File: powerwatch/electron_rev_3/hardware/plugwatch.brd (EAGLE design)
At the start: 57.1 x 93 mm, 123 parts, among them J1 DM3AT-SF-PEJM5, J2 TC2030-JLINK-NL, U1 BGA725L6-ALT, U10 SIP32510, U11 SIP32510, U12 SIP32510, U13 SIP32510, U14 MPU-9250, U15 OPA322AIDBVT, U2 SAFFB1G56KB0F0A, U3 ISL29035, U4 MAX-M8, U5 MAX740XESA, U6 SIP32510, U7 NRF51822QF, U8 OPA322AIDBVT, U9 SIP32510, X1 32.768k, X2 16MHz

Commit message: small changes
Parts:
- moved U$3 15.0 mm to (32.5, 1.02)
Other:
- board text added: "PowerWatch Noah Klugman Branden Ghena Neal Jackson Josh Adkins Rev 3, 03/18"
- board text removed: "Noah Klugman Branden Ghena Neal Jackson Rev 3 03/18"
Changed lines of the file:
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@@
 <?xml version="1.0" encoding="utf-8"?>
 <!DOCTYPE eagle SYSTEM "eagle.dtd">
-<eagle version="8.5.1">
+<eagle version="8.7.1">
 <drawing>
 <settings>
@@
 <wire x1="43.561" y1="23.368" x2="45.466" y2="23.368" width="0.127" layer="21"/>
 <text x="44.704" y="53.34" size="0.8128" layer="25" font="vector" ratio="12" rot="R270" align="bottom-center">!LIGHT_INT</text>
-<text x="28.448" y="4.064" size="1.016" layer="25" font="vector" ratio="12">Noah Klugman
+<text x="39.624" y="1.016" size="1.016" layer="25" font="vector" ratio="12">PowerWatch
+Noah Klugman
 Branden Ghena
 Neal Jackson
-Rev 3
-03/18</text>
+Josh Adkins
+Rev 3, 03/18</text>
 <text x="44.704" y="90.424" size="0.8128" layer="25" font="vector" ratio="12" align="bottom-center">WIFI_PWR_EN</text>
 <text x="46.736" y="41.656" size="0.8128" layer="25" font="vector" ratio="12" rot="R180" align="bottom-center">AUDIO_OUT</text>
@@
 <text x="8.89" y="52.578" size="0.8128" layer="25" font="vector" ratio="12" rot="R270" align="bottom-center">BLE_TXD</text>
 <text x="9.144" y="20.32" size="1.27" layer="25" font="vector" ratio="12" align="bottom-center">SD CARD</text>
-<text x="47.498" y="73.914" size="1.778" layer="25" font="vector" ratio="12">APN</text>
+<text x="47.752" y="73.914" size="1.778" layer="25" font="vector" ratio="12">APN</text>
 <text x="47.752" y="72.644" size="0.8128" layer="25" font="vector" ratio="12">(on, on)</text>
 </plain>
@@
 <attribute name="VALUE" x="23.622" y="34.036" size="1.016" layer="27" font="vector" ratio="12" align="bottom-center"/>
 </element>
-<element name="U$3" library="logos" package="UCB_CAL_200MIL" value="" x="18.542" y="6.604" smashed="yes"/>
+<element name="U$3" library="logos" package="UCB_CAL_200MIL" value="" x="32.512" y="1.016" smashed="yes"/>
 <element name="U10" library="chips" package="TSOT23-6" value="SIP32510" x="37.084" y="45.212" smashed="yes" rot="MR0">
 <attribute name="DIGIKEY" value=" SIP32510DT-T1-GE3CT-ND" x="37.084" y="45.212" size="1.778" layer="27" display="off"/>

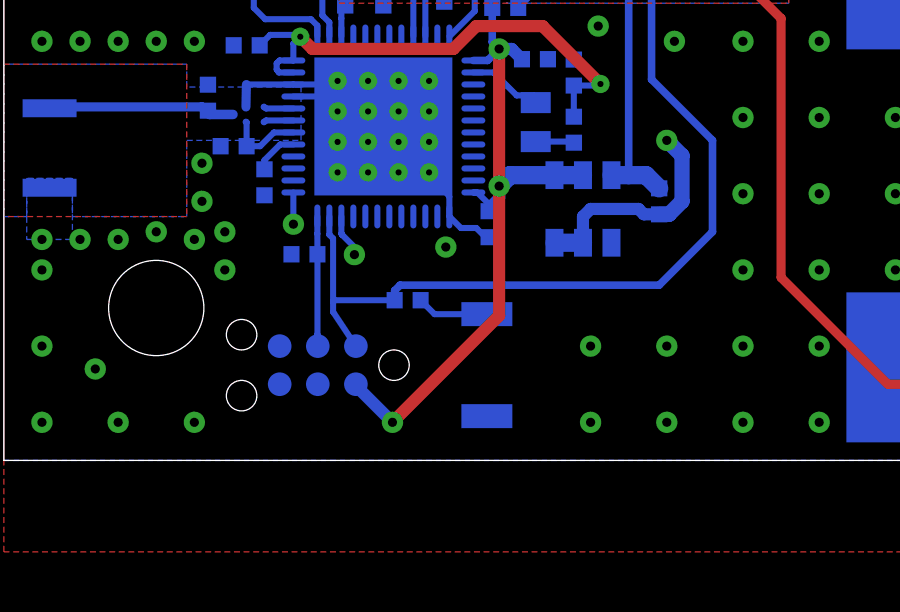
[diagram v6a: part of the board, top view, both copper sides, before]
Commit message: moved programmer and reset for NRF
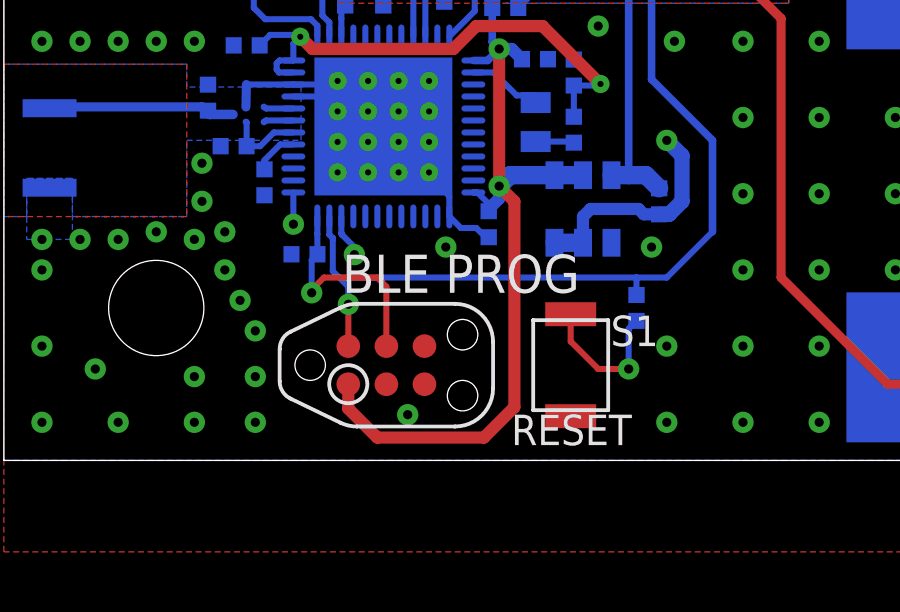
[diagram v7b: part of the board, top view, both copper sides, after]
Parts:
- moved R2 7.63 mm to (21.1, 5.08), turned to 270 degrees
- moved S1 2.79 mm to (18.9, 3.17), flipped to the top
- moved J2 2.29 mm to (12.8, 3.17), flipped to the top
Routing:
- net VCC_BLE: track 24.1 -> 27.8 mm, vias 3 -> 2
- net NRF_SWDCLK: track 4.32 -> 7.63 mm, vias 0 -> 1
- net N$26: track 2.40 -> 4.93 mm, vias 0 -> 1
- net NRF_SWDIO/!RESET: track 68.0 -> 67.8 mm, vias 0 -> 1
- net GND: vias 201 -> 206
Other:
- board text added: "BLE PROG"
- board text removed: "BLE"

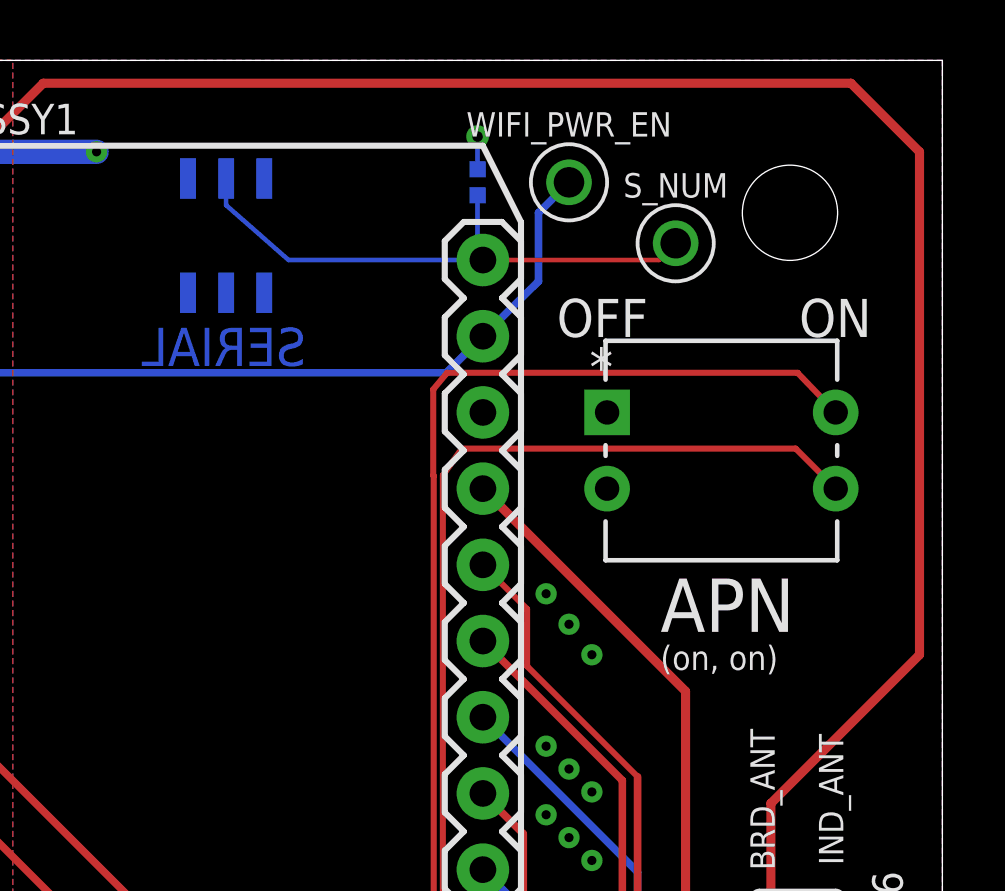
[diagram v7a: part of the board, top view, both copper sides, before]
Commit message: fixed library parts and added pulldowns
specifically
    - made sure origins were at the center of the part
    - fixed ds2401p+ lan pattern to match maxim spec
    - changed text ratios to 12
    - changed attribute fields to match rest of BOM
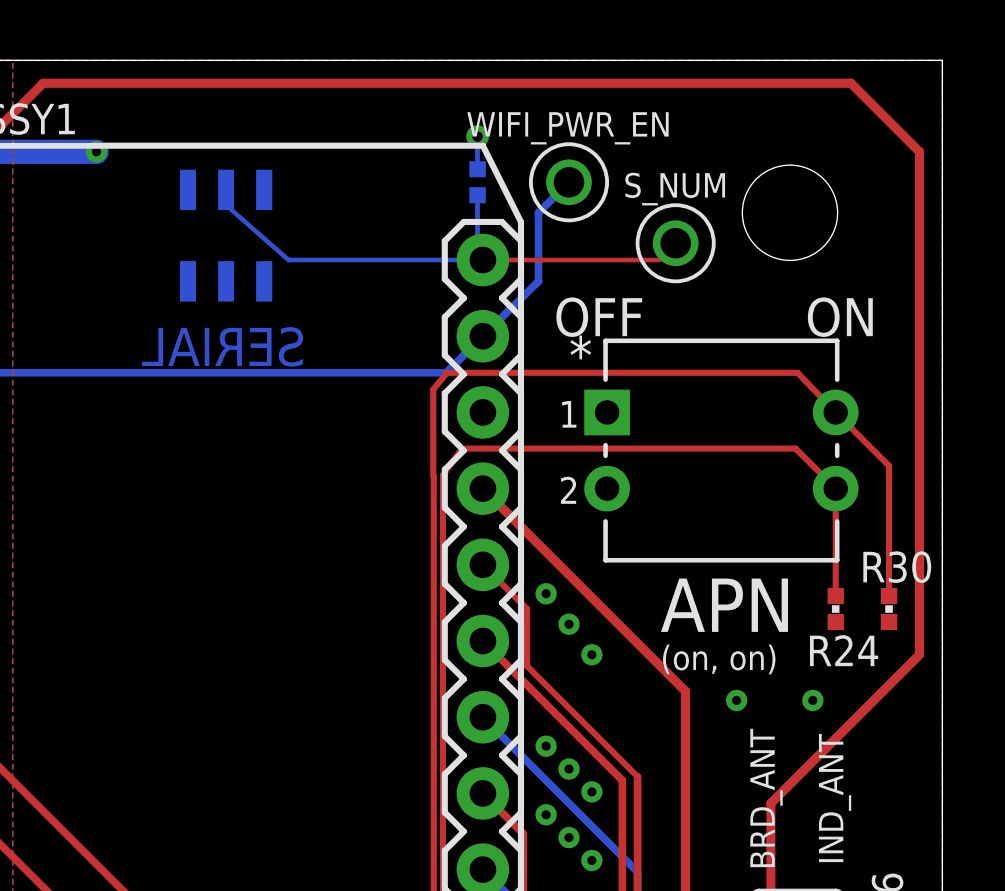
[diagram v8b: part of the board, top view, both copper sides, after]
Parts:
- added R24, R30: 10k, passives:0402_RES
- S1: value (none) -> B3U-1000P
- moved APN_SWITCH 4.02 mm to (49.8, 80.0)
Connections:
- net APN_DIP_1: now also R30.2
- net APN_DIP_2: now also R24.2
- net GND: now also R24.1, R30.1
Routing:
- net APN_DIP_1: track 43.6 -> 50.5 mm
- net APN_DIP_2: track 37.9 -> 41.5 mm
- net GND: vias 206 -> 208
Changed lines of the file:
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@@
 <attribute name="VALUE" x="7.493" y="73.66" size="1.016" layer="28" font="vector" ratio="12" rot="MR90" align="bottom-center"/>
 </element>
-<element name="S1" library="switches" package="B3U-1000P" value="" x="18.8946" y="3.175" smashed="yes" rot="R90">
+<element name="S1" library="switches" package="B3U-1000P" value="B3U-1000P" x="18.8946" y="3.175" smashed="yes" rot="R90">
 <attribute name="DIGIKEY" value="SW1020CT-ND" x="18.8946" y="3.175" size="1.778" layer="28" rot="MR0" display="off"/>
 <attribute name="MANUFACTURER" value="Omron" x="18.8946" y="3.175" size="1.778" layer="28" rot="MR0" display="off"/>
@@
 <attribute name="NAME" x="51.308" y="33.909" size="1.016" layer="26" font="vector" ratio="12" rot="MR0" align="top-center"/>
 </element>
-<element name="U4" library="u-blox" package="MAX-M8" value="MAX-M8" x="35.306" y="31.242" smashed="yes" rot="MR90">
+<element name="U4" library="u-blox" library_urn="urn:adsk.eagle:library:406" package="MAX-M8" value="MAX-M8" x="35.306" y="31.242" smashed="yes" rot="MR90">
 <attribute name="DESCRIPTION" value="IC RECEIVER GPS/GNSS 18LCC" x="35.306" y="31.242" size="1.778" layer="27" display="off"/>
 <attribute name="DIGIKEY" value="672-1003-1-ND" x="35.306" y="31.242" size="1.778" layer="27" display="off"/>
@@
 <element name="X1" library="crystals" package="ABS05" value="32.768k" x="13.716" y="17.4244" smashed="yes" rot="MR180">
 <attribute name="DIGIKEY" value="535-11897-1-ND" x="13.716" y="17.4244" size="1.778" layer="27" display="off"/>
+<attribute name="MANUFACTURER" value="Abracon" x="13.716" y="17.4244" size="1.778" layer="28" rot="MR180" display="off"/>
+<attribute name="MPN" value="ABS05-32.768KHZ-9-T" x="13.716" y="17.4244" size="1.778" layer="28" rot="MR180" display="off"/>
 <attribute name="NAME" x="13.716" y="18.0228" size="1.016" layer="26" font="vector" ratio="12" rot="MR0" align="bottom-center"/>
 <attribute name="VALUE" x="13.716" y="19.1244" size="1.016" layer="28" font="vector" ratio="12" rot="MR180" align="bottom-center"/>
@@
 </element>
 <element name="SERIAL" library="DS2401P+" package="21-0382" value="DS2401P+" x="33.274" y="87.122" smashed="yes" rot="MR270">
-<attribute name="MANUFACTURER_PART_NUMBER" value="DS2401P+" x="33.274" y="87.122" size="1.778" layer="28" rot="MR270" display="off"/>
+<attribute name="DIGIKEY" value="DS2401P+-ND" x="33.274" y="87.122" size="1.778" layer="28" rot="MR270" display="off"/>
+<attribute name="MANUFACTURER" value="Maxim Integrated" x="33.274" y="87.122" size="1.778" layer="28" rot="MR270" display="off"/>
+<attribute name="MPN" value="DS2401P+" x="33.274" y="87.122" size="1.778" layer="28" rot="MR270" display="off"/>
 <attribute name="NAME" x="35.941" y="82.7786" size="1.27" layer="16" font="vector" ratio="12" rot="SMR0"/>
-<attribute name="VENDOR" value="Maxim Integrated Products" x="33.274" y="87.122" size="1.778" layer="28" rot="MR270" display="off"/>
 </element>
 <element name="R29" library="passives" package="0402_RES" value="5K" x="41.656" y="88.9" smashed="yes" rot="MR270">
@@
 <attribute name="VALUE" x="43.053" y="88.9" size="1.016" layer="28" font="vector" ratio="12" rot="MR270" align="bottom-center"/>
 </element>
-<element name="APN_SWITCH" library="18250571" package="SWDIP4_300X138P100" value="1825057-1" x="53.594" y="78.6892" smashed="yes">
-<attribute name="MANUFACTURER_PART_NUMBER" value="18250571" x="53.594" y="78.6892" size="1.778" layer="27" display="off"/>
-<attribute name="VENDOR" value="TE Connectivity" x="53.594" y="78.6892" size="1.778" layer="27" display="off"/>
+<element name="APN_SWITCH" library="18250571" package="SWDIP4_300X138P100" value="1825057-1" x="49.784" y="79.9592" smashed="yes">
+<attribute name="DIGIKEY" value="450-1363-ND" x="49.784" y="79.9592" size="1.778" layer="27" display="off"/>
+<attribute name="MANUFACTURER" value="TE Connectivity" x="49.784" y="79.9592" size="1.778" layer="27" display="off"/>
+<attribute name="MPN" value="18250571" x="49.784" y="79.9592" size="1.778" layer="27" display="off"/>
+</element>
+<element name="R24" library="passives" package="0402_RES" value="10k" x="53.594" y="74.676" smashed="yes" rot="R90">
+<attribute name="DESCRIPTION" value="RES SMD 10K OHM 1% 1/16W 0402" x="53.594" y="74.676" size="1.778" layer="27" font="vector" ratio="12" rot="R90" display="off"/>
+<attribute name="DIGIKEY" value="RMCF0402FT10K0CT-ND" x="53.594" y="74.676" size="1.778" layer="27" font="vector" ratio="12" rot="R90" display="off"/>
+<attribute name="MANUFACTURER" value="Stackpole Electronics" x="53.594" y="74.676" size="1.778" layer="27" font="vector" ratio="12" rot="R90" display="off"/>
+<attribute name="MPN" value="RMCF0402FT10K0" x="53.594" y="74.676" size="1.778" layer="27" font="vector" ratio="12" rot="R90" display="off"/>
+<attribute name="NAME" x="53.848" y="73.787" size="1.016" layer="25" font="vector" ratio="12" rot="R180" align="bottom-center"/>
+<attribute name="VALUE" x="54.991" y="74.676" size="1.016" layer="27" font="vector" ratio="12" rot="R90" align="bottom-center"/>
+</element>
+<element name="R30" library="passives" package="0402_RES" value="10k" x="55.372" y="74.676" smashed="yes" rot="R90">
+<attribute name="DESCRIPTION" value="RES SMD 10K OHM 1% 1/16W 0402" x="55.372" y="74.676" size="1.778" layer="27" font="vector" ratio="12" rot="R90" display="off"/>
+<attribute name="DIGIKEY" value="RMCF0402FT10K0CT-ND" x="55.372" y="74.676" size="1.778" layer="27" font="vector" ratio="12" rot="R90" display="off"/>
+<attribute name="MANUFACTURER" value="Stackpole Electronics" x="55.372" y="74.676" size="1.778" layer="27" font="vector" ratio="12" rot="R90" display="off"/>
+<attribute name="MPN" value="RMCF0402FT10K0" x="55.372" y="74.676" size="1.778" layer="27" font="vector" ratio="12" rot="R90" display="off"/>
+<attribute name="NAME" x="55.626" y="76.581" size="1.016" layer="25" font="vector" ratio="12" rot="R180" align="bottom-center"/>
+<attribute name="VALUE" x="56.769" y="74.676" size="1.016" layer="27" font="vector" ratio="12" rot="R90" align="bottom-center"/>
 </element>
 </elements>
@@
 <via x="21.59" y="7.112" extent="1-16" drill="0.3048"/>
 <via x="13.462" y="1.524" extent="1-16" drill="0.3048"/>
+<contactref element="R24" pad="1"/>
+<contactref element="R30" pad="1"/>
+<via x="50.292" y="71.628" extent="1-16" drill="0.3048"/>
+<via x="52.832" y="71.628" extent="1-16" drill="0.3048"/>
 </signal>
 <signal name="GPS_PWR_EN">
@@
 <wire x1="52.324" y1="82.55" x2="40.64" y2="82.55" width="0.2032" layer="1"/>
 <wire x1="40.64" y1="82.55" x2="40.178846875" y2="81.995153125" width="0.2032" layer="1"/>
+<contactref element="R30" pad="2"/>
+<wire x1="55.372" y1="75.10906875" x2="55.372" y2="79.4512" width="0.2032" layer="1"/>
+<wire x1="55.372" y1="79.4512" x2="53.594" y2="81.2292" width="0.2032" layer="1"/>
 </signal>
 <signal name="APN_DIP_2">
@@
 <wire x1="40.5003" y1="79.13634375" x2="41.13265625" y2="80.0227" width="0.2032" layer="1"/>
 <wire x1="40.5003" y1="57.51565625" x2="40.5003" y2="79.13634375" width="0.2032" layer="1"/>
-<wire x1="52.2605" y1="80.0227" x2="53.594" y2="78.6892" width="0.2032" layer="1"/>
+<wire x1="52.2605" y1="80.0227" x2="53.4416" y2="78.8416" width="0.2032" layer="1"/>
 <wire x1="41.13265625" y1="80.0227" x2="52.2605" y2="80.0227" width="0.2032" layer="1"/>
 <wire x1="41.8338" y1="55.8292" x2="40.5003" y2="57.51565625" width="0.2032" layer="1"/>
+<contactref element="R24" pad="2"/>
+<wire x1="53.594" y1="75.10906875" x2="53.594" y2="78.6892" width="0.2032" layer="1"/>
+<wire x1="53.594" y1="78.6892" x2="53.4416" y2="78.8416" width="0.2032" layer="1"/>
 </signal>
 <signal name="SERIAL_NUM">
@@
 <wire x1="41.8338" y1="86.3092" x2="35.3568" y2="86.3092" width="0.1524" layer="16"/>
 <wire x1="35.3568" y1="86.3092" x2="33.274" y2="88.138" width="0.1524" layer="16"/>
-<wire x1="33.274" y1="88.138" x2="33.274" y2="89.027" width="0.1524" layer="16"/>
+<wire x1="33.274" y1="88.138" x2="33.274" y2="88.647" width="0.1524" layer="16"/>
 <wire x1="41.8338" y1="86.3092" x2="41.656" y2="86.487" width="0.1524" layer="16"/>
 <wire x1="41.656" y1="86.487" x2="41.656" y2="88.46693125" width="0.1524" layer="16"/>
@@
 which will not be processed correctly with this version.
 </note>
+<note version="8.2" severity="warning">
+Since Version 8.2, EAGLE supports online libraries. The ids
+of those online libraries will not be understood (or retained)
+with this version.
+</note>
 </compatibility>
